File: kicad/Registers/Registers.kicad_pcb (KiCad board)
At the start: 2 copper layers, 206.4 x 137.5 mm, 59 parts, among them J1 Control Connector, J2 Data Connector, U1 74LS253, U10 74LS244, U11 74LS244, U12 74LS244, U13 74LS377, U14 74LS377, U15 74LS377, U16 74LS377, U17 74LS377, U18 74LS377, U19 74LS169, U2 74LS253, U20 74LS169, U21 74LS283, U22 74LS283, U23 74LS283, U24 74LS283, U25 74LS32, U26 74LS02, U27 74LS32, U3 74LS253, U4 74LS253, U5 74LS253, U6 74LS253, U7 74LS253, U8 74LS253, U9 74LS253

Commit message: Gerber creation marathon
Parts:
- moved C1 44.5 mm to (232.3, 68.6)
- moved C2 44.5 mm to (209.5, 68.6)
- moved C3 44.5 mm to (187.2, 68.6)
- moved C4 44.5 mm to (163.8, 68.6)
- moved C5 44.5 mm to (140.9, 68.6)
- moved C6 44.5 mm to (118.0, 68.6)
- moved C7 44.5 mm to (95.2, 68.6)
- moved C8 44.5 mm to (72.3, 68.6)
- moved C9 44.5 mm to (49.5, 68.6)
- moved U1 44.4 mm to (226.1, 71.8)
- moved U2 44.4 mm to (203.2, 71.8)
- moved U3 44.4 mm to (180.3, 71.8)
- moved U4 44.4 mm to (157.5, 71.8)
- moved U5 44.4 mm to (134.6, 71.8)
- moved U6 44.4 mm to (111.8, 71.8)
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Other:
- board text removed: "JLCJLCJLCJLC"

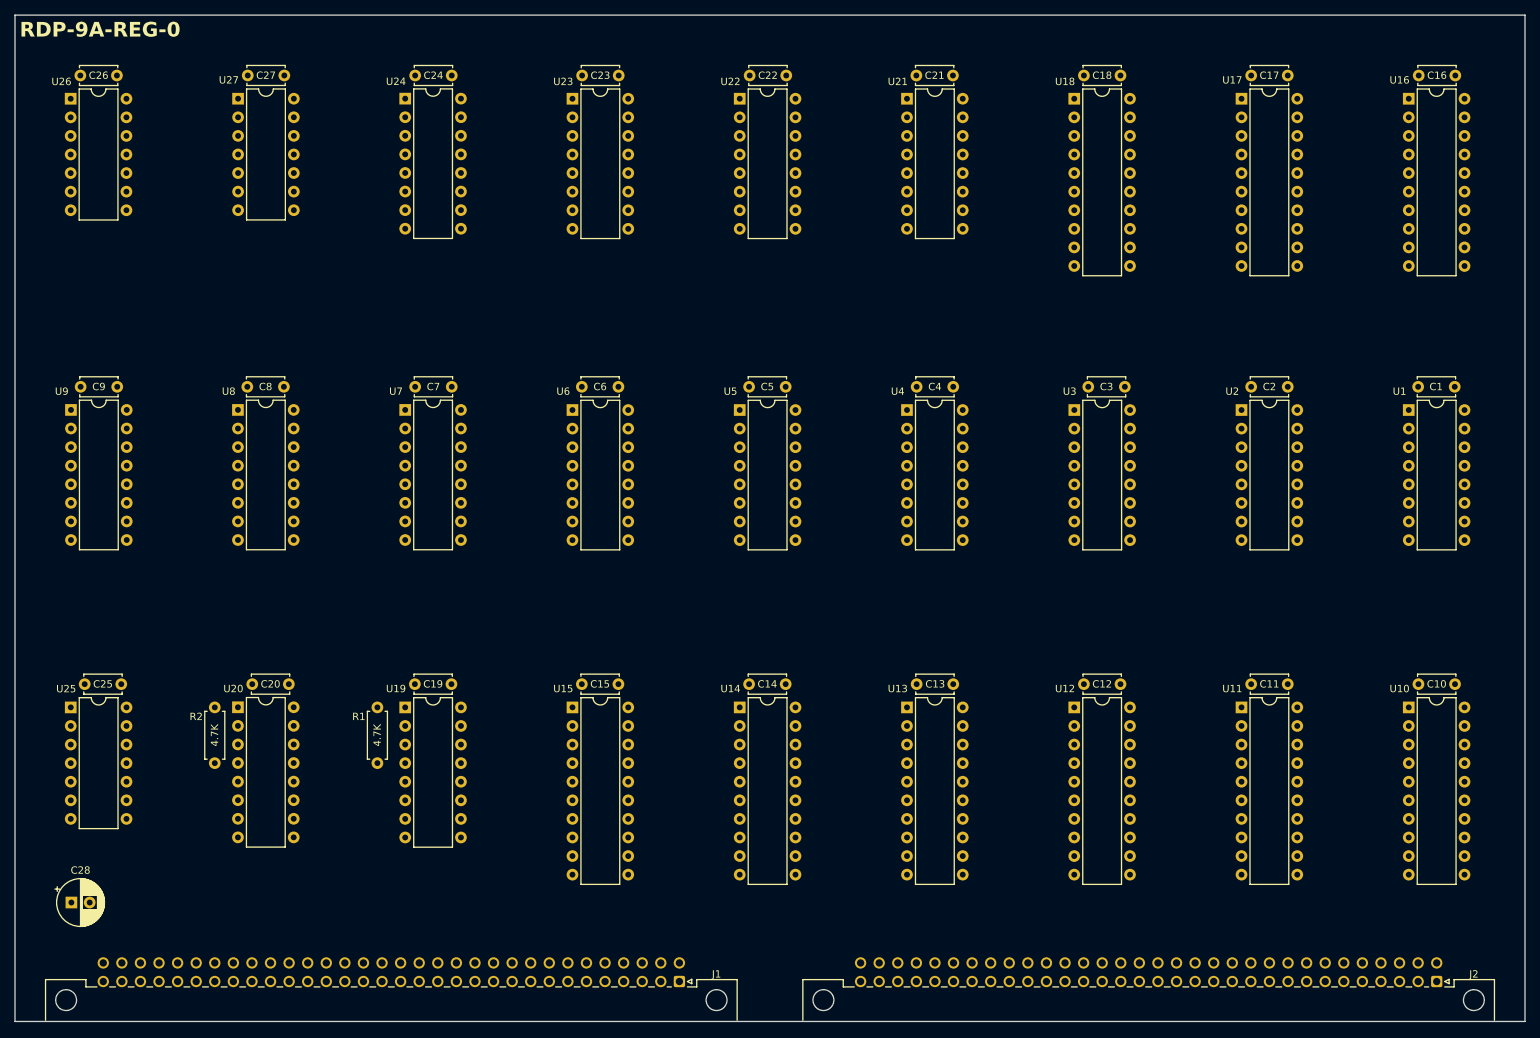
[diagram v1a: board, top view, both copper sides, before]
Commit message: Create gerber for register file
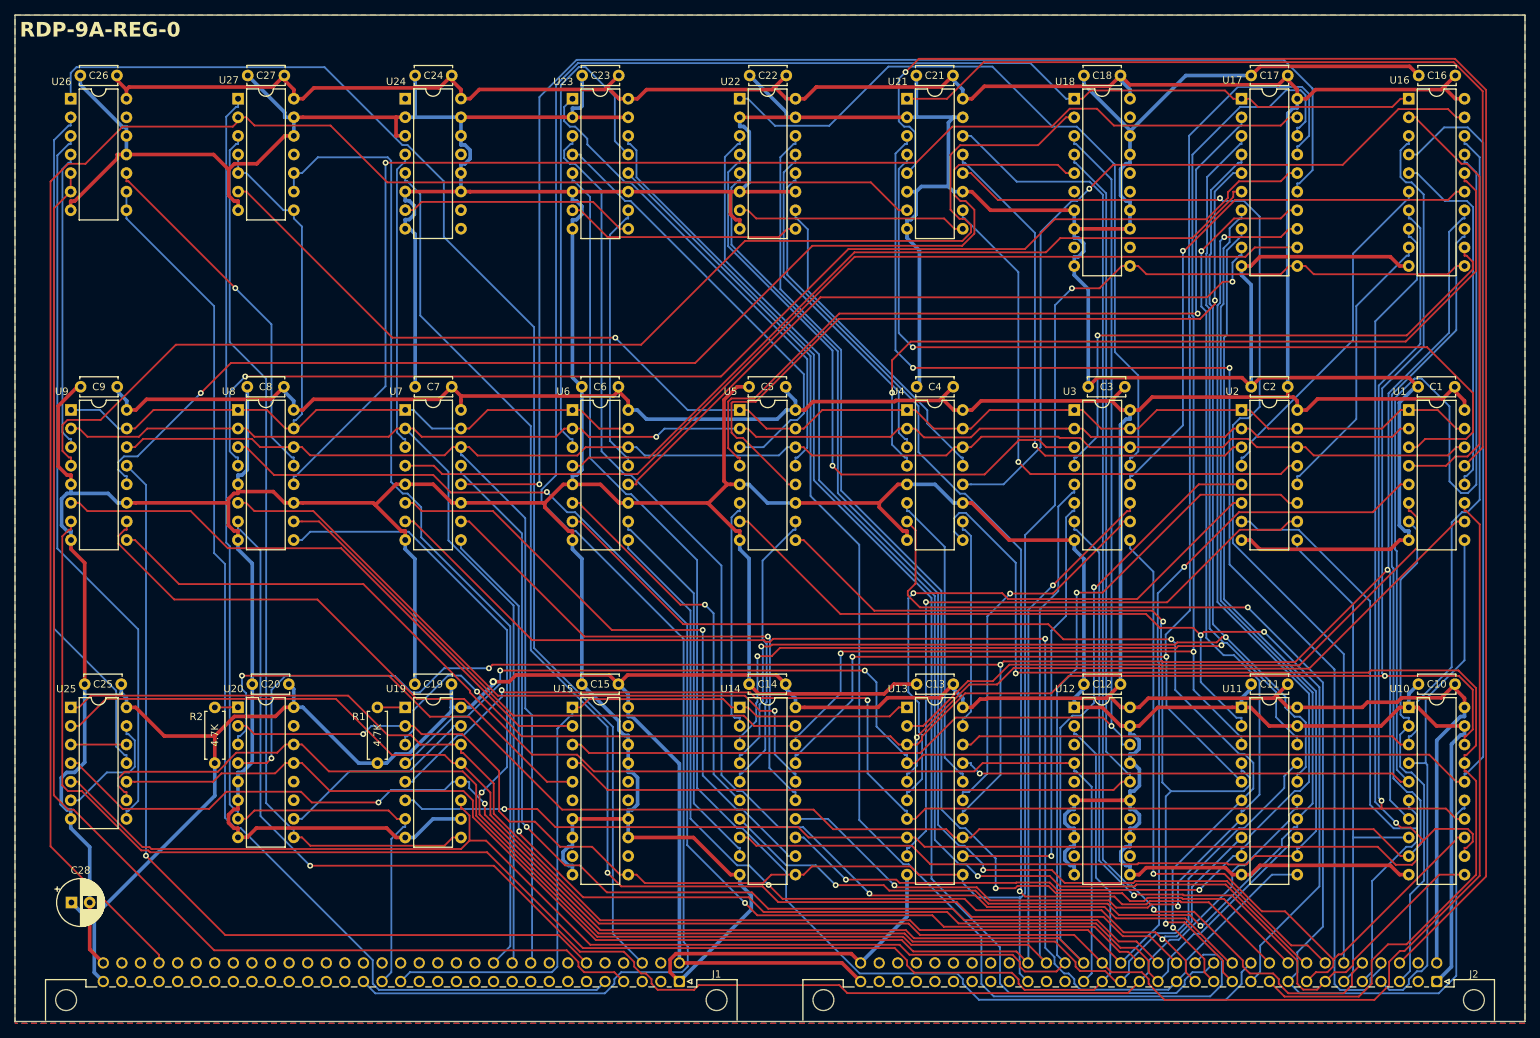
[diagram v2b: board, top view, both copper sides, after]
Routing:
- net GND: track 0.00 -> 1437.3 mm
- net +5V: track 0.00 -> 882.8 mm, vias 0 -> 1
- net /*LATCH_MQ: track 0.00 -> 298.6 mm
- net /DB5: track 0.00 -> 287.8 mm, vias 0 -> 4
- net /CLK: track 0.00 -> 278.3 mm, vias 0 -> 2
- net /SC1: track 0.00 -> 274.2 mm
- net /DB4: track 0.00 -> 273.6 mm, vias 0 -> 1
- net /BUS_SELECT1: track 0.00 -> 269.6 mm, vias 0 -> 1
- net /BUS_SELECT0: track 0.00 -> 265.3 mm
- net /DB1: track 0.00 -> 263.6 mm, vias 0 -> 2
- net /SC0: track 0.00 -> 255.6 mm, vias 0 -> 1
- net /DB2: track 0.00 -> 250.8 mm, vias 0 -> 3
- net /DB0: track 0.00 -> 247.7 mm, vias 0 -> 2
- net /DB3: track 0.00 -> 246.7 mm, vias 0 -> 2
- net /SC3: track 0.00 -> 243.0 mm, vias 0 -> 1
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- added copper zone on B.Cu, net GND
- added copper zone on F.Cu, net GND
